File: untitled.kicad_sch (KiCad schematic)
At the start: 11 parts, among them U1 HPM5E31IPB1

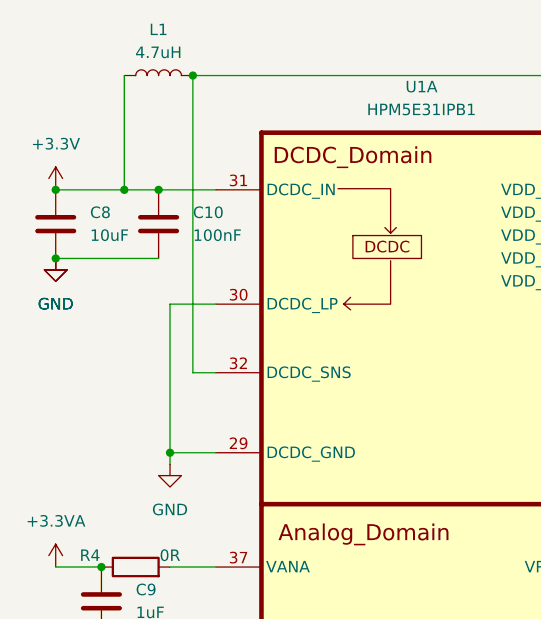
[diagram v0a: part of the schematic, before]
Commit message: 修改错误引脚
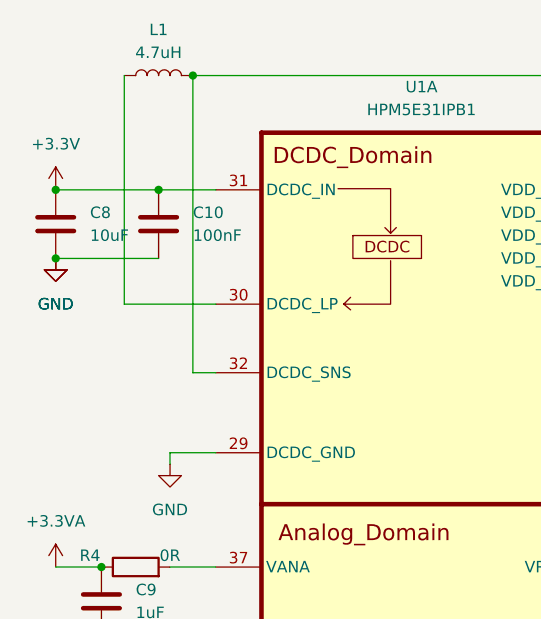
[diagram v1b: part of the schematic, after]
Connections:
- net +3.3V: no longer L1.2
- net GND: no longer U1.30 (DCDC_LP)
- new net: L1.2, U1.30 (DCDC_LP)
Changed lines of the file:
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@@
-	)
-	(junction
-		(at 64.77 85.09)
-		(diameter 0)
-		(color 0 0 0 0)
 	)
 	(junction
@@
 		(color 0 0 0 0)
 	)
-	(junction
-		(at 69.85 114.3)
-		(diameter 0)
-		(color 0 0 0 0)
-	)
 	(wire
 		(pts
@@
 	(wire
 		(pts
-			(xy 69.85 97.79) (xy 69.85 114.3)
-		)
-		(stroke
-			(width 0)
-			(type default)
-		)
-	)
-	(wire
-		(pts
 			(xy 123.19 92.71) (xy 123.19 95.25)
 		)
@@
 	(wire
 		(pts
+			(xy 64.77 72.39) (xy 64.77 97.79)
+		)
+		(stroke
+			(width 0)
+			(type default)
+		)
+	)
+	(wire
+		(pts
 			(xy 130.81 87.63) (xy 130.81 96.52)
 		)
@@
 	(wire
 		(pts
-			(xy 64.77 72.39) (xy 64.77 85.09)
-		)
-		(stroke
-			(width 0)
-			(type default)
-		)
-	)
-	(wire
-		(pts
 			(xy 143.51 111.76) (xy 148.59 111.76)
 		)
@@
 	(wire
 		(pts
-			(xy 57.15 85.09) (xy 64.77 85.09)
+			(xy 72.39 72.39) (xy 72.39 105.41)
+		)
+		(stroke
+			(width 0)
+			(type default)
+		)
+	)
+	(wire
+		(pts
+			(xy 57.15 85.09) (xy 68.58 85.09)
 		)
 		(stroke
@@
 	(wire
 		(pts
-			(xy 64.77 85.09) (xy 68.58 85.09)
-		)
-		(stroke
-			(width 0)
-			(type default)
-		)
-	)
-	(wire
-		(pts
 			(xy 125.73 92.71) (xy 125.73 106.68)
 		)
@@
 	(wire
 		(pts
-			(xy 74.93 97.79) (xy 69.85 97.79)
-		)
-		(stroke
-			(width 0)
-			(type default)
-		)
-	)
-	(wire
-		(pts
 			(xy 69.85 127) (xy 74.93 127)
 		)
@@
 	(wire
 		(pts
-			(xy 72.39 72.39) (xy 72.39 105.41)
-		)
-		(stroke
-			(width 0)
-			(type default)
-		)
-	)
-	(wire
-		(pts
 			(xy 123.19 92.71) (xy 125.73 92.71)
 		)
@@
 		)
 		(stroke
+			(width 0)
+			(type default)
+		)
+	)
+	(wire
+		(pts
+			(xy 74.93 97.79) (xy 64.77 97.79)
+		)
+		(stroke
